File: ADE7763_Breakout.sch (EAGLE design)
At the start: 24 parts, among them J1 10p-2.54, Q1 3.58MHz, U1 ADE7763ARSZ

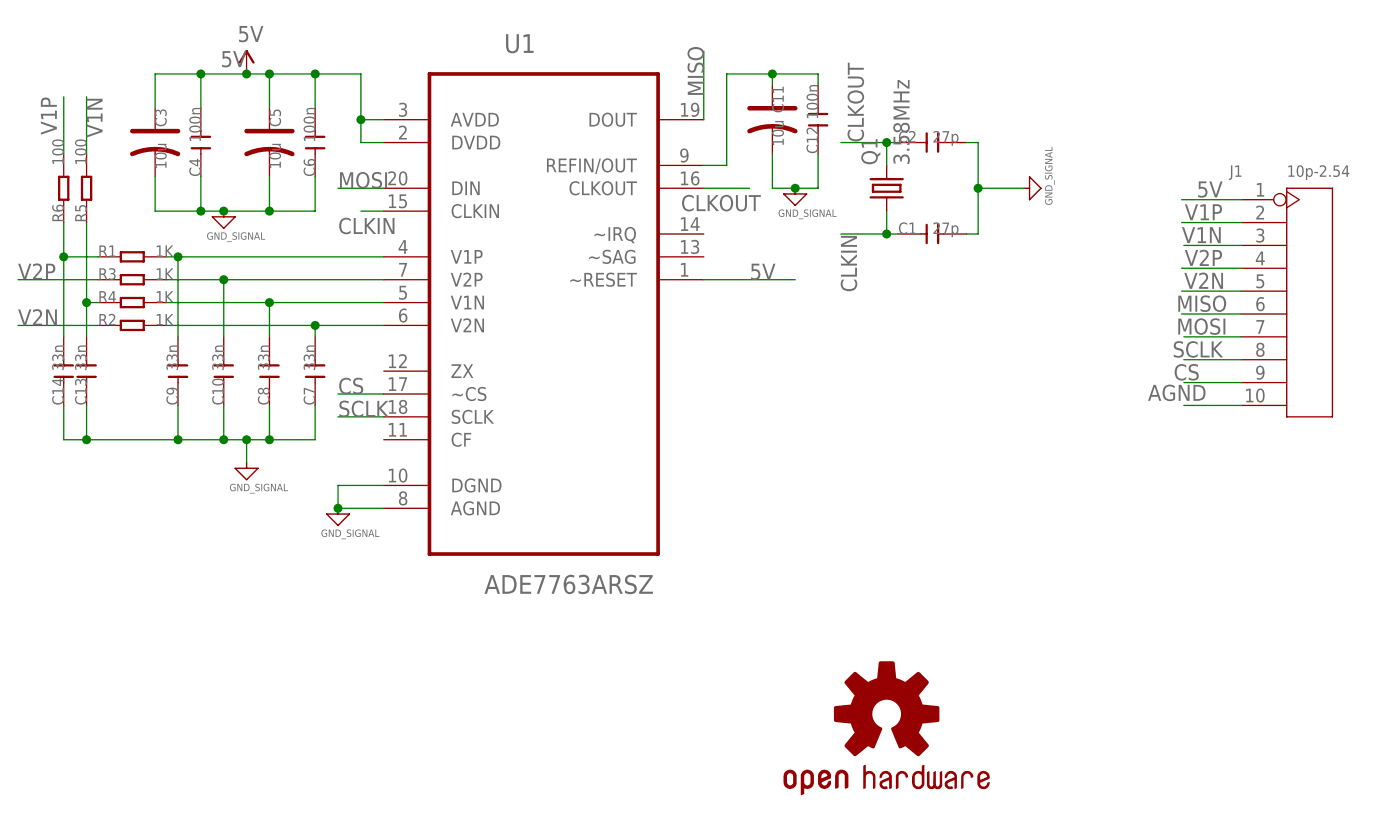
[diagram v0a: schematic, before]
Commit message: Corrected footprint and labels, added wirepads for other pins
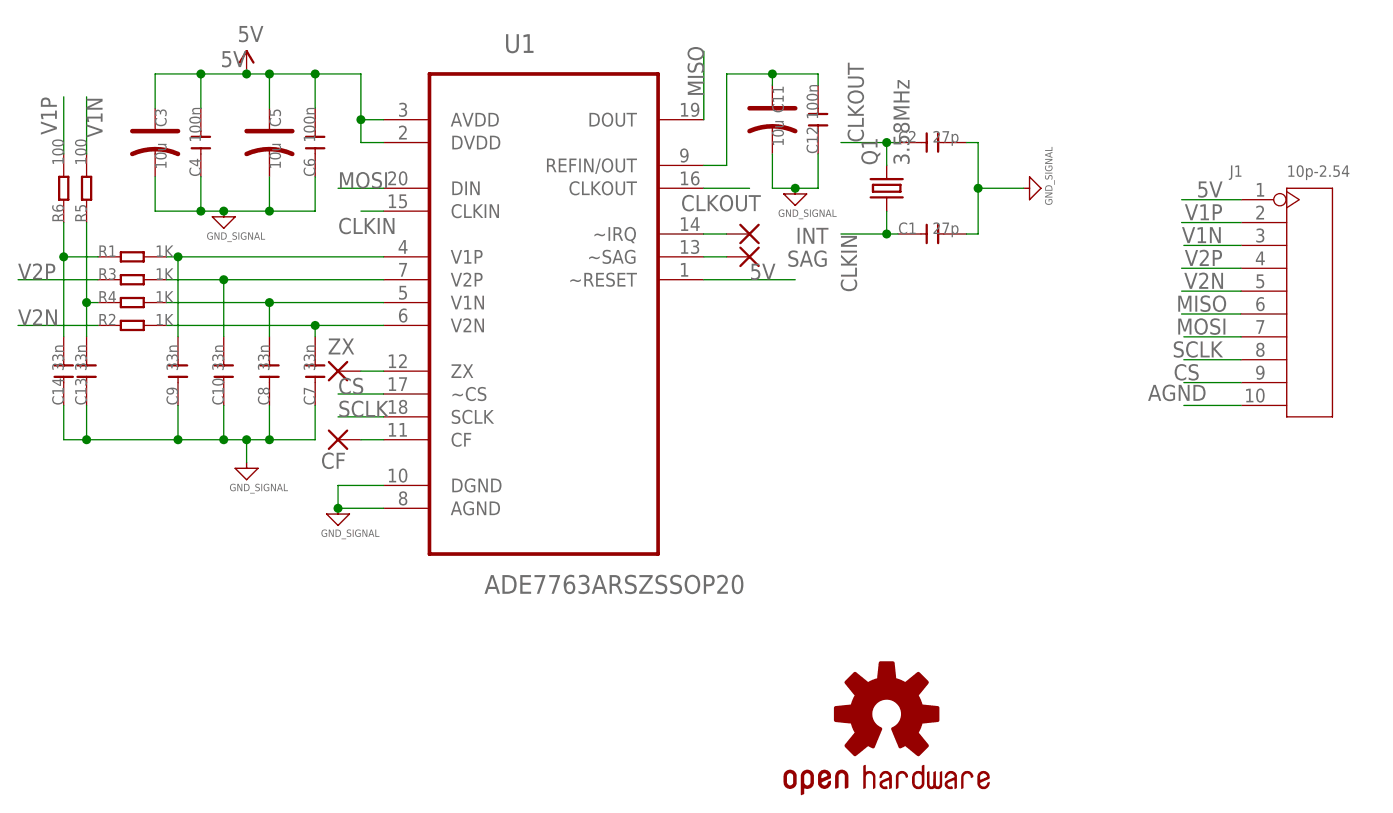
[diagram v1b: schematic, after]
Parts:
- added CF, INT, SAG, ZX: WIREPADSMD1,27-254, wirepad:WIREPADSMD1,27-254
- U1: value ADE7763ARSZ -> ADE7763ARSZSSOP20; device Analog Devices_By_element14_Batch_1:ADE7763ARSZ -> Analog Devices_By_element14_Batch_1:ADE7763ARSZSSOP20
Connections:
- new net N$10: U1.ZX, ZX.P
- new net N$11: CF.P, U1.CF
- new net N$3: INT.P, U1.~IRQ
- new net N$8: SAG.P, U1.~SAG
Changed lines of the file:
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@@
 <grid distance="0.1" unitdist="inch" unit="inch" style="lines" multiple="1" display="no" altdistance="0.01" altunitdist="inch" altunit="inch"/>
 <layers>
-<layer number="1" name="Top" color="4" fill="1" visible="no" active="no"/>
-<layer number="16" name="Bottom" color="1" fill="1" visible="no" active="no"/>
-<layer number="17" name="Pads" color="2" fill="1" visible="no" active="no"/>
-<layer number="18" name="Vias" color="2" fill="1" visible="no" active="no"/>
-<layer number="19" name="Unrouted" color="6" fill="1" visible="no" active="no"/>
-<layer number="20" name="Dimension" color="15" fill="1" visible="no" active="no"/>
-<layer number="21" name="tPlace" color="7" fill="1" visible="no" active="no"/>
-<layer number="22" name="bPlace" color="7" fill="1" visible="no" active="no"/>
-<layer number="23" name="tOrigins" color="15" fill="1" visible="no" active="no"/>
-<layer number="24" name="bOrigins" color="15" fill="1" visible="no" active="no"/>
-<layer number="25" name="tNames" color="7" fill="1" visible="no" active="no"/>
-<layer number="26" name="bNames" color="7" fill="1" visible="no" active="no"/>
-<layer number="27" name="tValues" color="7" fill="1" visible="no" active="no"/>
-<layer number="28" name="bValues" color="7" fill="1" visible="no" active="no"/>
+<layer number="1" name="Top" color="4" fill="1" visible="yes" active="no"/>
+<layer number="16" name="Bottom" color="1" fill="1" visible="yes" active="no"/>
+<layer number="17" name="Pads" color="2" fill="1" visible="yes" active="no"/>
+<layer number="18" name="Vias" color="2" fill="1" visible="yes" active="no"/>
+<layer number="19" name="Unrouted" color="6" fill="1" visible="yes" active="no"/>
+<layer number="20" name="Dimension" color="15" fill="1" visible="yes" active="no"/>
+<layer number="21" name="tPlace" color="7" fill="1" visible="yes" active="no"/>
+<layer number="22" name="bPlace" color="7" fill="1" visible="yes" active="no"/>
+<layer number="23" name="tOrigins" color="15" fill="1" visible="yes" active="no"/>
+<layer number="24" name="bOrigins" color="15" fill="1" visible="yes" active="no"/>
+<layer number="25" name="tNames" color="7" fill="1" visible="yes" active="no"/>
+<layer number="26" name="bNames" color="7" fill="1" visible="yes" active="no"/>
+<layer number="27" name="tValues" color="7" fill="1" visible="yes" active="no"/>
+<layer number="28" name="bValues" color="7" fill="1" visible="yes" active="no"/>
 <layer number="29" name="tStop" color="7" fill="3" visible="no" active="no"/>
 <layer number="30" name="bStop" color="7" fill="6" visible="no" active="no"/>
@@
 <layer number="35" name="tGlue" color="7" fill="4" visible="no" active="no"/>
 <layer number="36" name="bGlue" color="7" fill="5" visible="no" active="no"/>
-<layer number="37" name="tTest" color="7" fill="1" visible="no" active="no"/>
-<layer number="38" name="bTest" color="7" fill="1" visible="no" active="no"/>
+<layer number="37" name="tTest" color="7" fill="1" visible="yes" active="no"/>
+<layer number="38" name="bTest" color="7" fill="1" visible="yes" active="no"/>
 <layer number="39" name="tKeepout" color="4" fill="11" visible="no" active="no"/>
 <layer number="40" name="bKeepout" color="1" fill="11" visible="no" active="no"/>
@@
 <layer number="44" name="Drills" color="7" fill="1" visible="no" active="no"/>
 <layer number="45" name="Holes" color="7" fill="1" visible="no" active="no"/>
-<layer number="46" name="Milling" color="3" fill="1" visible="no" active="no"/>
-<layer number="47" name="Measures" color="7" fill="1" visible="no" active="no"/>
-<layer number="48" name="Document" color="7" fill="1" visible="no" active="no"/>
-<layer number="49" name="Reference" color="7" fill="1" visible="no" active="no"/>
-<layer number="50" name="dxf" color="7" fill="1" visible="no" active="no"/>
-<layer number="51" name="tDocu" color="7" fill="1" visible="no" active="no"/>
-<layer number="52" name="bDocu" color="7" fill="1" visible="no" active="no"/>
-<layer number="53" name="tGND_GNDA" color="7" fill="9" visible="no" active="no"/>
-<layer number="54" name="bGND_GNDA" color="1" fill="9" visible="no" active="no"/>
-<layer number="56" name="wert" color="7" fill="1" visible="no" active="no"/>
-<layer number="57" name="tCAD" color="7" fill="1" visible="no" active="no"/>
+<layer number="46" name="Milling" color="3" fill="1" visible="yes" active="no"/>
+<layer number="47" name="Measures" color="7" fill="1" visible="yes" active="no"/>
+<layer number="48" name="Document" color="7" fill="1" visible="yes" active="no"/>
+<layer number="49" name="Reference" color="7" fill="1" visible="yes" active="no"/>
+<layer number="50" name="dxf" color="7" fill="1" visible="yes" active="no"/>
+<layer number="51" name="tDocu" color="7" fill="1" visible="yes" active="no"/>
+<layer number="52" name="bDocu" color="7" fill="1" visible="yes" active="no"/>
+<layer number="53" name="tGND_GNDA" color="7" fill="9" visible="yes" active="no"/>
+<layer number="54" name="bGND_GNDA" color="1" fill="9" visible="yes" active="no"/>
+<layer number="56" name="wert" color="7" fill="1" visible="yes" active="no"/>
+<layer number="57" name="tCAD" color="7" fill="1" visible="yes" active="no"/>
 <layer number="90" name="Modules" color="5" fill="1" visible="yes" active="yes"/>
 <layer number="91" name="Nets" color="2" fill="1" visible="yes" active="yes"/>
@@
 </classes>
 <parts>
-<part name="U1" library="Analog Devices_By_element14_Batch_1" deviceset="ADE7763ARSZ" device=""/>
+<part name="U1" library="Analog Devices_By_element14_Batch_1" deviceset="ADE7763ARSZ" device="SSOP20" value="ADE7763ARSZSSOP20"/>
 <part name="FRAME1" library="SparkFun-Aesthetics" deviceset="FRAME-A4L" device=""/>
 <part name="Q1" library="crystal" deviceset="CRYSTAL" device="HC49UP" value="3.58MHz"/>
@@
 <part name="SUPPLY1" library="SparkFun-Aesthetics" deviceset="5V" device=""/>
 <part name="LOGO1" library="SparkFun-Aesthetics" deviceset="OSHW-LOGO" device="M"/>
+<part name="INT" library="wirepad" deviceset="WIREPAD" device="SMD1,27-254" value="WIREPADSMD1,27-254"/>
+<part name="ZX" library="wirepad" deviceset="WIREPAD" device="SMD1,27-254" value="WIREPADSMD1,27-254"/>
+<part name="SAG" library="wirepad" deviceset="WIREPAD" device="SMD1,27-254" value="WIREPADSMD1,27-254"/>
+<part name="CF" library="wirepad" deviceset="WIREPAD" device="SMD1,27-254" value="WIREPADSMD1,27-254"/>
 </parts>
 <sheets>
@@
 <instance part="SUPPLY1" gate="G$1" x="27.94" y="132.08"/>
 <instance part="LOGO1" gate="G$1" x="99.06" y="60.96"/>
+<instance part="INT" gate="G$1" x="83.82" y="114.3" smashed="yes" rot="R180">
+<attribute name="NAME" x="92.583" y="114.9858" size="1.778" layer="95" rot="R180"/>
+</instance>
+<instance part="ZX" gate="G$1" x="38.1" y="99.06" smashed="yes">
+<attribute name="NAME" x="36.957" y="100.9142" size="1.778" layer="95"/>
+</instance>
+<instance part="SAG" gate="G$1" x="83.82" y="111.76" smashed="yes" rot="R180">
+<attribute name="NAME" x="92.583" y="112.4458" size="1.778" layer="95" rot="R180"/>
+</instance>
+<instance part="CF" gate="G$1" x="38.1" y="91.44" smashed="yes">
+<attribute name="NAME" x="36.195" y="88.2142" size="1.778" layer="95"/>
+</instance>
 </instances>
 <busses>
@@
 </segment>
 </net>
+<net name="N$3" class="0">
+<segment>
+<pinref part="U1" gate="A" pin="~IRQ"/>
+<pinref part="INT" gate="G$1" pin="P"/>
+<wire x1="78.74" y1="114.3" x2="81.28" y2="114.3" width="0.1524" layer="91"/>
+</segment>
+</net>
+<net name="N$8" class="0">
+<segment>
+<pinref part="U1" gate="A" pin="~SAG"/>
+<pinref part="SAG" gate="G$1" pin="P"/>
+<wire x1="78.74" y1="111.76" x2="81.28" y2="111.76" width="0.1524" layer="91"/>
+</segment>
+</net>
+<net name="N$10" class="0">
+<segment>
+<pinref part="ZX" gate="G$1" pin="P"/>
+<pinref part="U1" gate="A" pin="ZX"/>
+<wire x1="40.64" y1="99.06" x2="43.18" y2="99.06" width="0.1524" layer="91"/>
+</segment>
+</net>
+<net name="N$11" class="0">
+<segment>
+<pinref part="CF" gate="G$1" pin="P"/>
+<pinref part="U1" gate="A" pin="CF"/>
+<wire x1="40.64" y1="91.44" x2="43.18" y2="91.44" width="0.1524" layer="91"/>
+</segment>
+</net>
